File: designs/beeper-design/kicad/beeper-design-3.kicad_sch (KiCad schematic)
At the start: 30 parts, among them U12 DRV2605YZFR, U13 CSD75207W15, U3 BQ51003YFPR

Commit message: another export
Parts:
- removed C14: 2.2u, beeper-design:Pkg0201_18, symbol C335106_9
- removed C15: 2.2u, beeper-design:Pkg0201_11, symbol C335106_5
- removed C16: 2.2u, beeper-design:Pkg0201_27, symbol C335106_17
- removed C17: 2.2u, beeper-design:Pkg0201_40, symbol C335106_26
- removed C18: 2.2u, beeper-design:Pkg0201_53, symbol C335106_35
- removed C19: 2.2u, beeper-design:Pkg0201_10, symbol C335106_4
- removed C20: 2.2u, beeper-design:Pkg0201_26, symbol C335106_16
- removed C21: 2.2u, beeper-design:Pkg0201_39, symbol C335106_25
- removed C22: 2.2u, beeper-design:Pkg0201_52, symbol C335106_34
- removed C23: 2.2u, beeper-design:Pkg0201_9, symbol C335106_3
- removed C24: 2.2u, beeper-design:Pkg0201_23, symbol C335106_13
- removed C25: 2.2u, beeper-design:Pkg0201_16, symbol C335106_7
- removed C47: 2.2u, beeper-design:Pkg0201_35, symbol C335106_23
- removed C48: 2.2u, beeper-design:Pkg0201_47, symbol C335106_29
- removed R16, R17: 8K2, beeper-design:Pkg0201_8, symbol my_resistor_3
- removed R2: 845R, beeper-design:Pkg0201_32, symbol my_resistor_7
- removed R3: 10K, beeper-design:Pkg0201_30, symbol my_resistor_6
- removed R4: 20K, beeper-design:Pkg0201_2, symbol my_resistor
- removed R5: 10K, beeper-design:Pkg0201_15, symbol my_resistor_4
- removed R6: 196R, beeper-design:Pkg0201_45, symbol C138167
- removed R7: 10K, beeper-design:Pkg0201_41, symbol my_resistor_9
- removed R8: 1K, beeper-design:Pkg0201_54, symbol my_resistor_12
- removed TP1, TP13, TP14, TP2: (no value), beeper-design:SMD_TESTPT, symbol smd_testpoint_cmp
- removed U12: DRV2605YZFR, beeper-design:LP_8, symbol DRV2605YZFR
- removed U13: CSD75207W15, beeper-design:LP_6, symbol CSD75207W15
- removed U3: BQ51003YFPR, beeper-design:LP_7, symbol BQ51003YFPR
- added C13: 2.2u, beeper-design:Pkg0201_34, symbol C335106_24
- added U2: AT25FF321A-UUN-T, beeper-design:WLCSP_12, symbol AT25FF321A_UUN_T
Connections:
- net GND: now also C13.1, U2.C3 (GND)
- new net: U2.A1 (NC), U2.A5 (NC), U2.G1 (NC), U2.G5 (NC)
- new net V18F: C13.2, U2.B2 (Vcc)
- new net mcu_mcu-mem_cs: U2.B4 (CSn)
- new net mcu_mcu-mem_sck: U2.F2 (SCK)
- new net mcu_mcu-mem_sdio0: U2.E3 (SI)
- new net mcu_mcu-mem_sdio1: U2.D4 (SO)
- new net mcu_mcu-mem_sdio2: U2.F4 (WPn)
- new net mcu_mcu-mem_sdio3: U2.D2 (HRn)

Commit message: new export
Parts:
- removed C13: 2.2u, beeper-design:Pkg0201_34, symbol C335106_24
- added C13: 2.2u, beeper-design:Pkg0201_28, symbol C335106_18
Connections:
- net GND: now also C13.1
- net V18F: now also C13.2
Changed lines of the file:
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@@
     (instances
       (project "beeper-design"
-        (path "/26c9a8ce-e1cd-a3ff-a24b-a16076d913bd"
+        (path "/219df102-d28d-b743-245e-efc9439ef913"
           (reference "U2") (unit 1)
         )
@@
     )
   )
-  (symbol (lib_id "C335106_24") (at 231.14 110.49 180.0)  (unit 1)
+  (symbol (lib_id "C335106_18") (at 231.14 110.49 180.0)  (unit 1)
     (in_bom yes) (on_board yes)
     (property "Reference" "C13" (id 0) (at 229.87 109.22 0.0) (effects (font (size 0.762 0.762)) (justify left )))
     (property "Value" "2.2u" (id 1) (at 229.87 111.76 0.0) (effects (font (size 0.762 0.762)) (justify left )))
-    (property "Footprint" "beeper-design:Pkg0201_34" (id 2) (at 231.14 110.49 0.0) (effects (font (size 0.762 0.762)) hide))
+    (property "Footprint" "beeper-design:Pkg0201_28" (id 2) (at 231.14 110.49 0.0) (effects (font (size 0.762 0.762)) hide))
     (property "Datasheet" "https://datasheet.lcsc.com/lcsc/2304140030_Murata-Electronics-GRM033R61A225KE47D_C335106.pdf" (id 3) (at 231.14 110.49 0.0) (effects (font (size 0.762 0.762)) hide))
       (property "Name" "mcu_mem_cap" (id 4) (at 231.14 110.49 180.0) (effects (font (size 0.762 0.762)) hide))
@@
     (instances
       (project "beeper-design"
-        (path "/26c9a8ce-e1cd-a3ff-a24b-a16076d913bd"
+        (path "/219df102-d28d-b743-245e-efc9439ef913"
           (reference "C13") (unit 1)
         )
@@
     (instances
       (project "beeper-design"
-        (path "/26c9a8ce-e1cd-a3ff-a24b-a16076d913bd"
+        (path "/219df102-d28d-b743-245e-efc9439ef913"
           (reference "#PWR?") (unit 1)
         )
@@
     (instances
       (project "beeper-design"
-        (path "/26c9a8ce-e1cd-a3ff-a24b-a16076d913bd"
+        (path "/219df102-d28d-b743-245e-efc9439ef913"
           (reference "#PWR?") (unit 1)
         )

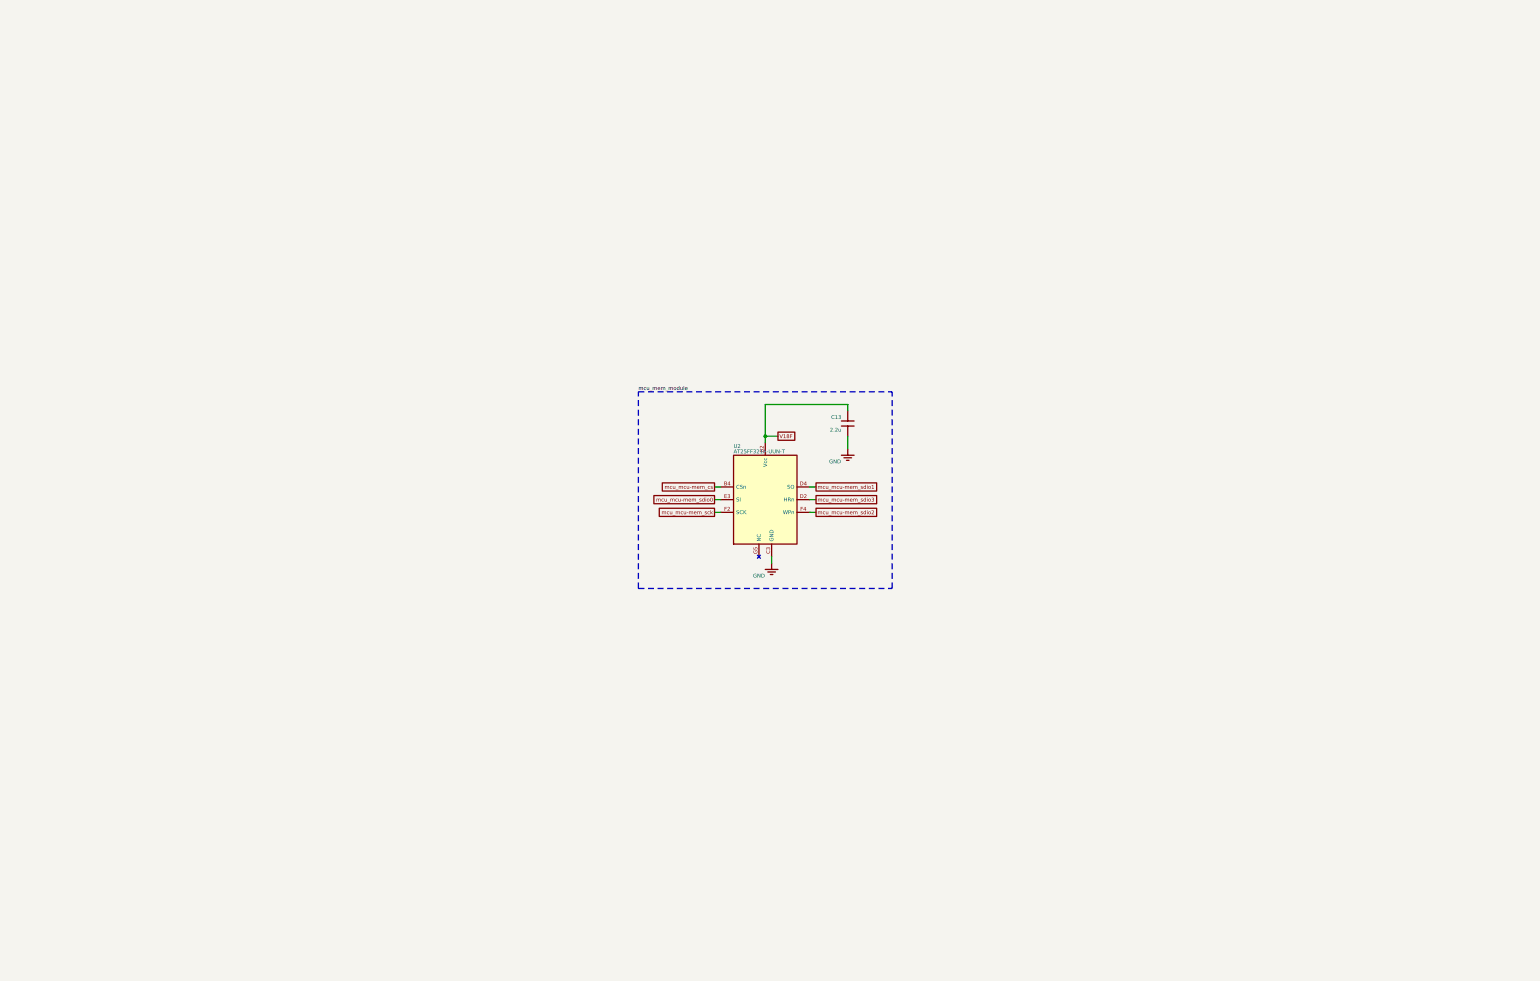
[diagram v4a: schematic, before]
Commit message: exported, yet XTALM32p keeps disappearing
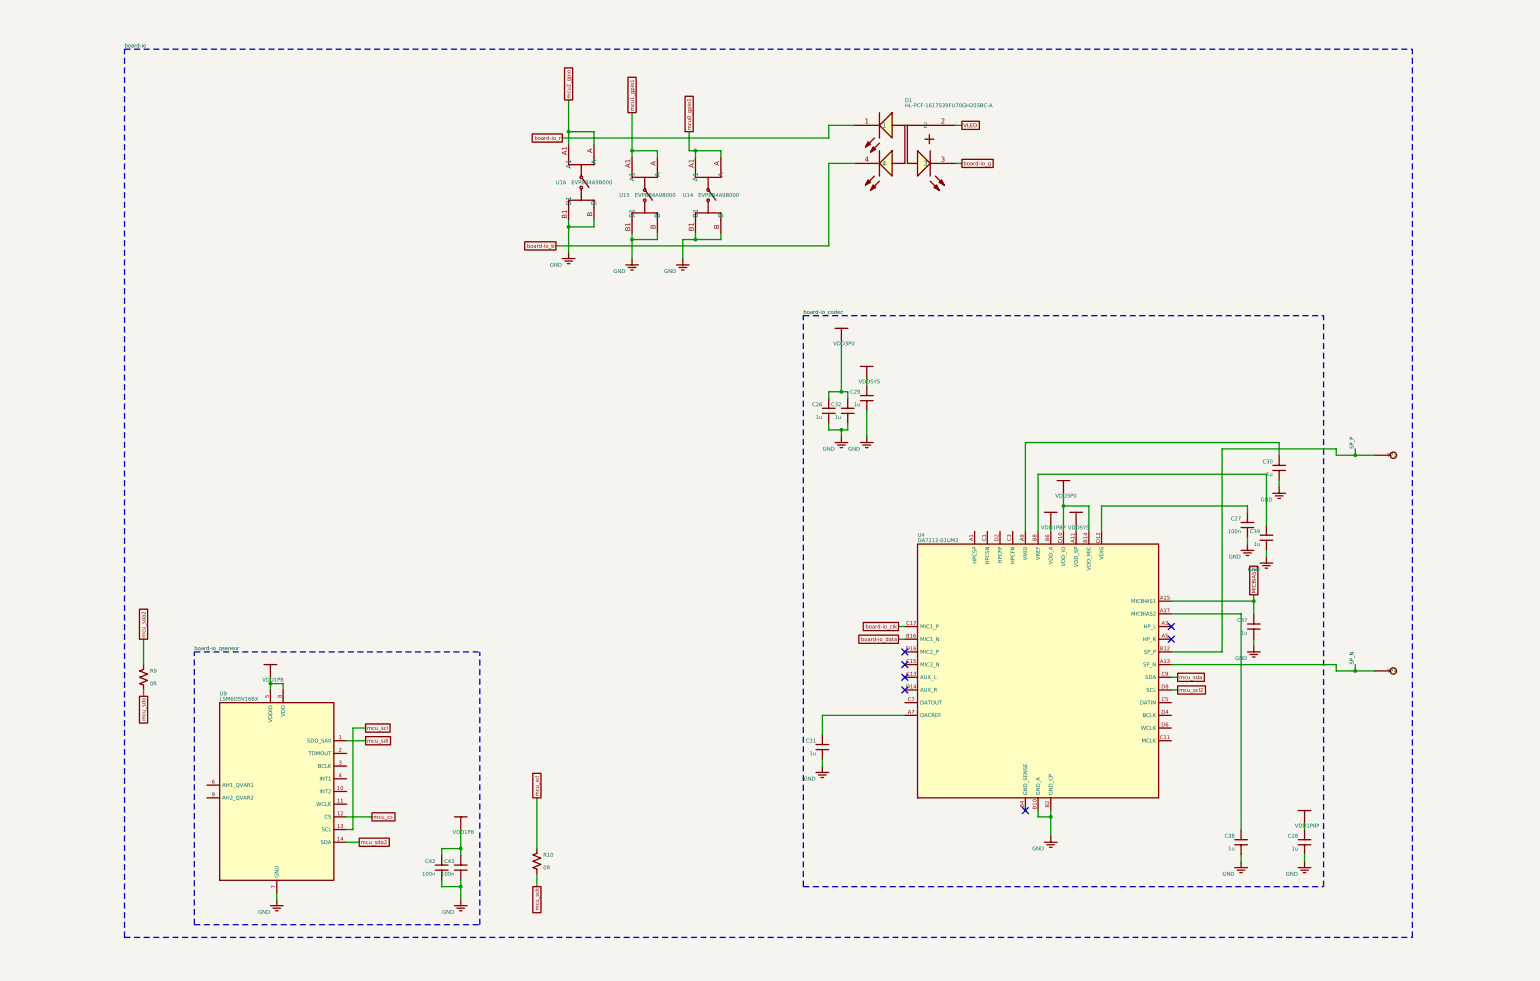
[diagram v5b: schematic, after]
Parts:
- removed C13: 2.2u, beeper-design:Pkg0201_28, symbol C335106_18
- removed U2: AT25FF321A-UUN-T, beeper-design:WLCSP_12, symbol AT25FF321A_UUN_T
- added C26: 1u, beeper-design:Pkg0201_43, symbol my_capacitor_25
- added C27: 100n, beeper-design:Pkg0201_46, symbol my_capacitor_26
- added C28: 1u, beeper-design:Pkg0201_38, symbol my_capacitor_22
- added C29: 1u, beeper-design:Pkg0201_13, symbol my_capacitor_7
- added C30: 1u, beeper-design:Pkg0201_31, symbol my_capacitor_17
- added C31: 1u, beeper-design:Pkg0201_35, symbol my_capacitor_21
- added C32: 1u, beeper-design:Pkg0201_6, symbol my_capacitor_4
- added C37: 1u, beeper-design:Pkg0201_18, symbol my_capacitor_10
- added C38: 1u, beeper-design:Pkg0201_24, symbol my_capacitor_13
- added C39: 1u, beeper-design:Pkg0201_1, symbol my_capacitor_1
- added C42: 100n, beeper-design:Pkg0201_34, symbol my_capacitor_20
- added C43: 100n, beeper-design:Pkg0201_41, symbol my_capacitor_24
- added D1: HL-PCF-1617S39FU70GH203BC-A, beeper-design:LP_5, symbol C513368
- added R10: 0R, beeper-design:Pkg0201_9, symbol my_resistor_4
- added R9: 0R, beeper-design:Pkg0201_3, symbol my_resistor_1
- added TP3, TP4: (no value), beeper-design:SMD_TESTPT, symbol smd_testpoint_cmp
- added U14, U15, U16: EVPBB4A9B000, beeper-design:LP_2, symbol C140848
- added U4: DA7212-01UM2, beeper-design:LP_3, symbol component_2
- added U9: LSM6DSV16BX, beeper-design:LP_1, symbol LSM6DSOXTR
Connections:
- net GND: now also C26.1, C27.1, C28.1, C29.1, C30.1, C31.1, C32.1, C37.1, C38.1, C39.1, C42.1, C43.1, U14.B, U14.B1, U15.B, U15.B1, U16.B, U16.B1, U4.B10 (GND_A), U4.B2 (GND_CP), U9.7 (GND)
- new net: C38.2, U4.A17 (MICBIAS2)
- new net: C30.2, U4.A9 (VMID)
- new net: C31.2, U4.A7 (DACREF)
- new net: C39.2, U4.B8 (VREF)
- new net: C27.2, U4.D12 (VDIG)
- new net MICBIAS1: C37.2, U4.A15 (MICBIAS1)
- new net SP_N: TP4.p, U4.A13 (SP_N)
- new net SP_P: TP3.p, U4.B12 (SP_P)
- new net VDD1P8: C42.2, C43.2, U9.5 (VDDIO), U9.8 (VDD)
- new net VDD1P8P: C28.2, U4.B6 (VDD_A)
- new net VDD3P0: C26.2, C32.2, U4.B14 (VDD_MIC), U4.D10 (VDD_IO)
- new net VDDSYS: C29.2, U4.A11 (VDD_SP)
- new net VLED: D1.2
- new net board-io_b: D1.4
- new net board-io_clk: U4.C17 (MIC1_P)
- new net board-io_data: U4.B16 (MIC1_N)
- new net board-io_g: D1.3
- new net board-io_r: D1.1
- new net mcu0_gpio1: U14.A, U14.A1
- new net mcu1_gpio1: U15.A, U15.A1
- new net mcu2_gpio: U16.A, U16.A1
- new net mcu_cs: U9.12 (CS)
- new net mcu_sck: R10.2
- new net mcu_scl: R10.1, U9.13 (SCL)
- new net mcu_scl2: U4.D8 (SCL)
- new net mcu_sda: U4.C9 (SDA)
- new net mcu_sda2: R9.1, U9.14 (SDA)
- new net mcu_sdi: U9.1 (SDO_SA0)
- new net mcu_sdo: R9.2
- no-connect marks 0 -> 7

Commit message: fixed up pours, keepout regions
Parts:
- removed C26: 1u, beeper-design:Pkg0201_43, symbol my_capacitor_25
- removed C27: 100n, beeper-design:Pkg0201_46, symbol my_capacitor_26
- removed C28: 1u, beeper-design:Pkg0201_38, symbol my_capacitor_22
- removed C29: 1u, beeper-design:Pkg0201_13, symbol my_capacitor_7
- removed C30: 1u, beeper-design:Pkg0201_31, symbol my_capacitor_17
- removed C31: 1u, beeper-design:Pkg0201_35, symbol my_capacitor_21
- removed C32: 1u, beeper-design:Pkg0201_6, symbol my_capacitor_4
- removed C37: 1u, beeper-design:Pkg0201_18, symbol my_capacitor_10
- removed C38: 1u, beeper-design:Pkg0201_24, symbol my_capacitor_13
- removed C39: 1u, beeper-design:Pkg0201_1, symbol my_capacitor_1
- removed C42: 100n, beeper-design:Pkg0201_34, symbol my_capacitor_20
- removed C43: 100n, beeper-design:Pkg0201_41, symbol my_capacitor_24
- removed R10: 0R, beeper-design:Pkg0201_9, symbol my_resistor_4
- removed R9: 0R, beeper-design:Pkg0201_3, symbol my_resistor_1
- added C26: 1u, beeper-design:Pkg0201_9, symbol my_capacitor_4
- added C27: 100n, beeper-design:Pkg0201_12, symbol my_capacitor_5
- added C28: 1u, beeper-design:Pkg0201_4, symbol my_capacitor_1
- added C29: 1u, beeper-design:Pkg0201_27, symbol my_capacitor_13
- added C30: 1u, beeper-design:Pkg0201_45, symbol my_capacitor_23
- added C31: 1u, beeper-design:Pkg0201_1, symbol my_capacitor
- added C32: 1u, beeper-design:Pkg0201_20, symbol my_capacitor_10
- added C37: 1u, beeper-design:Pkg0201_32, symbol my_capacitor_16
- added C38: 1u, beeper-design:Pkg0201_38, symbol my_capacitor_19
- added C39: 1u, beeper-design:Pkg0201_15, symbol my_capacitor_7
- added C42: 100n, beeper-design:Pkg0201, symbol my_capacitor_26
- added C43: 100n, beeper-design:Pkg0201_7, symbol my_capacitor_3
- added R10: 0R, beeper-design:Pkg0201_23, symbol my_resistor_9
- added R9: 0R, beeper-design:Pkg0201_17, symbol my_resistor_6
- D1: footprint beeper-design:LP_5 -> beeper-design:LP
- U14, U15, U16: footprint beeper-design:LP_2 -> beeper-design:LP_5
- U4: footprint beeper-design:LP_3 -> beeper-design:LP_6
- U9: footprint beeper-design:LP_1 -> beeper-design:LP_4
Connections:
- net GND: now also C26.1, C27.1, C28.1, C29.1, C30.1, C31.1, C32.1, C37.1, C38.1, C39.1, C42.1, C43.1
- net MICBIAS1: now also C37.2
- net VDD1P8: now also C42.2, C43.2
- net VDD1P8P: now also C28.2
- net VDD3P0: now also C26.2, C32.2
- net VDDSYS: now also C29.2
- net mcu_sck: now also R10.2
- net mcu_scl: now also R10.1
- net mcu_sda2: now also R9.1
- net mcu_sdo: now also R9.2
- net at U4.A17 (MICBIAS2): now also C38.2
- net at U4.A9 (VMID): now also C30.2
- net at U4.A7 (DACREF): now also C31.2
- net at U4.B8 (VREF): now also C39.2
- net at U4.D12 (VDIG): now also C27.2

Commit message: exported to Kicad, fixed Kicad, exported gerbers
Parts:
- removed C26: 1u, beeper-design:Pkg0201_9, symbol my_capacitor_4
- removed C27: 100n, beeper-design:Pkg0201_12, symbol my_capacitor_5
- removed C28: 1u, beeper-design:Pkg0201_4, symbol my_capacitor_1
- removed C29: 1u, beeper-design:Pkg0201_27, symbol my_capacitor_13
- removed C30: 1u, beeper-design:Pkg0201_45, symbol my_capacitor_23
- removed C31: 1u, beeper-design:Pkg0201_1, symbol my_capacitor
- removed C32: 1u, beeper-design:Pkg0201_20, symbol my_capacitor_10
- removed C37: 1u, beeper-design:Pkg0201_32, symbol my_capacitor_16
- removed C38: 1u, beeper-design:Pkg0201_38, symbol my_capacitor_19
- removed C39: 1u, beeper-design:Pkg0201_15, symbol my_capacitor_7
- removed C42: 100n, beeper-design:Pkg0201, symbol my_capacitor_26
- removed C43: 100n, beeper-design:Pkg0201_7, symbol my_capacitor_3
- removed R10: 0R, beeper-design:Pkg0201_23, symbol my_resistor_9
- removed R9: 0R, beeper-design:Pkg0201_17, symbol my_resistor_6
- removed U4: DA7212-01UM2, beeper-design:LP_6, symbol component_2
- added C26: 1u, beeper-design:Pkg0201_24, symbol my_capacitor_14
- added C27: 100n, beeper-design:Pkg0201_27, symbol my_capacitor_15
- added C28: 1u, beeper-design:Pkg0201_19, symbol my_capacitor_11
- added C29: 1u, beeper-design:Pkg0201_42, symbol my_capacitor_23
- added C30: 1u, beeper-design:Pkg0201_12, symbol my_capacitor_6
- added C31: 1u, beeper-design:Pkg0201_16, symbol my_capacitor_10
- added C32: 1u, beeper-design:Pkg0201_35, symbol my_capacitor_20
- added C37: 1u, beeper-design:Pkg0201_47, symbol my_capacitor_26
- added C38: 1u, beeper-design:Pkg0201_5, symbol my_capacitor_2
- added C39: 1u, beeper-design:Pkg0201_30, symbol my_capacitor_17
- added C42: 100n, beeper-design:Pkg0201_15, symbol my_capacitor_9
- added C43: 100n, beeper-design:Pkg0201_22, symbol my_capacitor_13
- added R10: 0R, beeper-design:Pkg0201_38, symbol my_resistor_11
- added R9: 0R, beeper-design:Pkg0201_32, symbol my_resistor_8
- added U4: DA7212-01UM2, beeper-design:LP_3, symbol component
- D1: footprint beeper-design:LP -> beeper-design:LP_5
- U14, U15, U16: footprint beeper-design:LP_5 -> beeper-design:LP_2
- U9: footprint beeper-design:LP_4 -> beeper-design:LP_1
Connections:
- net GND: now also C26.1, C27.1, C28.1, C29.1, C30.1, C31.1, C32.1, C37.1, C38.1, C39.1, C42.1, C43.1, U4.B10 (GND_A), U4.B2 (GND_CP)
- net MICBIAS1: now also C37.2, U4.A15 (MICBIAS1)
- net SP_N: now also U4.A13 (SP_N)
- net SP_P: now also U4.B12 (SP_P)
- net VDD1P8: now also C42.2, C43.2
- net VDD1P8P: now also C28.2, U4.B6 (VDD_A)
- net VDD3P0: now also C26.2, C32.2, U4.B14 (VDD_MIC), U4.D10 (VDD_IO)
- net VDDSYS: now also C29.2, U4.A11 (VDD_SP)
- net board-io_clk: now also U4.C17 (MIC1_P)
- net board-io_data: now also U4.B16 (MIC1_N)
- net mcu_sck: now also R10.2
- net mcu_scl: now also R10.1
- net mcu_scl2: now also U4.D8 (SCL)
- net mcu_sda: now also U4.C9 (SDA)
- net mcu_sda2: now also R9.1
- net mcu_sdo: now also R9.2
- new net: C30.2, U4.A9 (VMID)
- new net: C31.2, U4.A7 (DACREF)
- new net: C38.2, U4.A17 (MICBIAS2)
- new net: C39.2, U4.B8 (VREF)
- new net: C27.2, U4.D12 (VDIG)

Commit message: latest fully routed version
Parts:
- removed C26: 1u, beeper-design:Pkg0201_24, symbol my_capacitor_14
- removed C27: 100n, beeper-design:Pkg0201_27, symbol my_capacitor_15
- removed C28: 1u, beeper-design:Pkg0201_19, symbol my_capacitor_11
- removed C29: 1u, beeper-design:Pkg0201_42, symbol my_capacitor_23
- removed C30: 1u, beeper-design:Pkg0201_12, symbol my_capacitor_6
- removed C31: 1u, beeper-design:Pkg0201_16, symbol my_capacitor_10
- removed C37: 1u, beeper-design:Pkg0201_47, symbol my_capacitor_26
- removed C38: 1u, beeper-design:Pkg0201_5, symbol my_capacitor_2
- removed C39: 1u, beeper-design:Pkg0201_30, symbol my_capacitor_17
- removed C42: 100n, beeper-design:Pkg0201_15, symbol my_capacitor_9
- removed C43: 100n, beeper-design:Pkg0201_22, symbol my_capacitor_13
- removed R10: 0R, beeper-design:Pkg0201_38, symbol my_resistor_11
- removed R9: 0R, beeper-design:Pkg0201_32, symbol my_resistor_8
- added C26: 1u, beeper-design:Pkg0201_7, symbol my_capacitor_4
- added C27: 100n, beeper-design:Pkg0201_24, symbol my_capacitor_13
- added C28: 1u, beeper-design:Pkg0201_12, symbol my_capacitor_6
- added C29: 1u, beeper-design:Pkg0201_46, symbol my_capacitor_26
- added C30: 1u, beeper-design:Pkg0201_33, symbol my_capacitor_19
- added C31: 1u, beeper-design:Pkg0201_43, symbol my_capacitor_25
- added C37: 1u, beeper-design:Pkg0201_10, symbol my_capacitor_5
- added C38: 1u, beeper-design:Pkg0201_21, symbol my_capacitor_12
- added C39: 1u, beeper-design:Pkg0201_20, symbol my_capacitor_11
- added C42: 100n, beeper-design:Pkg0201_14, symbol my_capacitor_8
- added C43: 100n, beeper-design:Pkg0201_26, symbol my_capacitor_14
- added R10: 0R, beeper-design:Pkg0201_17, symbol my_resistor_6
- added R9: 0R, beeper-design:Pkg0201_8, symbol my_resistor_3
- D1: footprint beeper-design:LP_5 -> beeper-design:LP_4
- TP3, TP4: now not fitted; now left out of the parts list
- U14, U15, U16: footprint beeper-design:LP_2 -> beeper-design:LP_1
- U4: footprint beeper-design:LP_3 -> beeper-design:LP_2
- U9: footprint beeper-design:LP_1 -> beeper-design:LP
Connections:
- net GND: now also C26.1, C27.1, C28.1, C29.1, C30.1, C31.1, C37.1, C38.1, C39.1, C42.1, C43.1
- net MICBIAS1: now also C37.2
- net VDD1P8: now also C42.2, C43.2
- net VDD1P8P: now also C28.2
- net VDD3P0: now also C26.2
- net VDDSYS: now also C29.2
- net at U4.A9 (VMID): now also C30.2
- net at U4.A7 (DACREF): now also C31.2
- net at U4.A17 (MICBIAS2): now also C38.2
- net at U4.B8 (VREF): now also C39.2
- net at U4.D12 (VDIG): now also C27.2
- net board-io_b renamed board-io_rgb_b
- net board-io_clk renamed codec-pdm-net_clk
- net board-io_data renamed codec-pdm-net_data
- net board-io_g renamed board-io_rgb_g
- net board-io_r renamed board-io_rgb_r
- net mcu0_gpio1 renamed mcu_mcu-button0_gpio
- net mcu1_gpio1 renamed mcu_mcu-button1_gpio
- net mcu2_gpio renamed mcu_mcu-button2_gpio
- net mcu_cs renamed mcu_q-spi_cs
- net mcu_scl renamed mcu_q-i3c_scl
- net mcu_q-i3c_scl: now also R10.1
- net mcu_scl2 renamed codec-i2c-net_scl
- net mcu_sda renamed codec-i2c-net_sda
- net mcu_sda2 renamed mcu_q-i3c_sda
- net mcu_q-i3c_sda: now also R9.1
- net mcu_sdi renamed mcu_q-spi_sdi
- new net mcu_q-spi_sck: R10.2
- new net mcu_q-spi_sdo: R9.2
